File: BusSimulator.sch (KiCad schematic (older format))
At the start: 14 parts, among them U1 MPM3620, U2 MPM3620

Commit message: Finished 3v3 and 5V
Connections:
- net labels removed: Earth
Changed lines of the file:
@@
 	1700 1050 1700 1075
 $Comp
-L +5V #PWR06
+L +5V #PWR05
 U 1 1 59FAA2C5
 P 2350 2650
-F 0 "#PWR06" H 2350 2500 50  0001 C CNN
+F 0 "#PWR05" H 2350 2500 50  0001 C CNN
 F 1 "+5V" H 2350 2790 50  0000 C CNN
 F 2 "" H 2350 2650 50  0001 C CNN
@@
 $EndComp
 $Comp
-L GNDREF #PWR07
+L GNDREF #PWR06
 U 1 1 59FAACBA
 P 1475 4425
-F 0 "#PWR07" H 1475 4175 50  0001 C CNN
+F 0 "#PWR06" H 1475 4175 50  0001 C CNN
 F 1 "GNDREF" H 1475 4275 50  0000 C CNN
 F 2 "" H 1475 4425 50  0001 C CNN
@@
 $EndComp
 $Comp
-L GNDA #PWR08
+L GNDA #PWR07
 U 1 1 59FAACCC
 P 2300 6850
-F 0 "#PWR08" H 2300 6600 50  0001 C CNN
+F 0 "#PWR07" H 2300 6600 50  0001 C CNN
 F 1 "GNDA" H 2300 6700 50  0000 C CNN
 F 2 "" H 2300 6850 50  0001 C CNN
@@
 $EndComp
 $Comp
-L GNDA #PWR09
+L GNDA #PWR08
 U 1 1 59FAACD8
 P 950 6100
-F 0 "#PWR09" H 950 5850 50  0001 C CNN
+F 0 "#PWR08" H 950 5850 50  0001 C CNN
 F 1 "GNDA" H 950 5950 50  0000 C CNN
 F 2 "" H 950 6100 50  0001 C CNN
@@
 	1875 4800 2075 4800
 $Comp
-L GNDA #PWR010
+L GNDA #PWR09
 U 1 1 59FAACFB
 P 2450 4850
-F 0 "#PWR010" H 2450 4600 50  0001 C CNN
+F 0 "#PWR09" H 2450 4600 50  0001 C CNN
 F 1 "GNDA" H 2450 4700 50  0000 C CNN
 F 2 "" H 2450 4850 50  0001 C CNN
@@
 $EndComp
 $Comp
-L Earth #PWR011
-U 1 1 59FAAD09
-P 2150 6400
-F 0 "#PWR011" H 2150 6150 50  0001 C CNN
-F 1 "Earth" H 2150 6250 50  0001 C CNN
-F 2 "" H 2150 6400 50  0001 C CNN
-F 3 "" H 2150 6400 50  0001 C CNN
-	1    2150 6400
-	1    0    0    -1
-$EndComp
-$Comp
 L CAPH C3
 U 1 1 59FAAD0F
@@
 	0    1    1    0
 $EndComp
-$Comp
-L Earth #PWR012
-U 1 1 59FAAD15
-P 1475 4050
-F 0 "#PWR012" H 1475 3800 50  0001 C CNN
-F 1 "Earth" H 1475 3900 50  0001 C CNN
-F 2 "" H 1475 4050 50  0001 C CNN
-F 3 "" H 1475 4050 50  0001 C CNN
-	1    1475 4050
-	1    0    0    -1
-$EndComp
 Wire Wire Line
 	1650 4075 1650 4050
-Wire Wire Line
-	1650 4050 1475 4050
-$Comp
-L +3.3V #PWR013
+$Comp
+L +3.3V #PWR010
 U 1 1 59FAAF36
 P 2300 5650
-F 0 "#PWR013" H 2300 5500 50  0001 C CNN
+F 0 "#PWR010" H 2300 5500 50  0001 C CNN
 F 1 "+3.3V" H 2300 5790 50  0000 C CNN
 F 2 "" H 2300 5650 50  0001 C CNN
@@
 PCE3900CT-ND
 $Comp
-L GNDREF #PWR014
+L GNDREF #PWR011
 U 1 1 59FACA7B
 P 2650 2400
-F 0 "#PWR014" H 2650 2150 50  0001 C CNN
+F 0 "#PWR011" H 2650 2150 50  0001 C CNN
 F 1 "GNDREF" H 2650 2250 50  0000 C CNN
 F 2 "" H 2650 2400 50  0001 C CNN
@@
 	2200 2400 2650 2400
 $Comp
-L GNDREF #PWR015
+L GNDREF #PWR012
 U 1 1 59FACBAF
 P 2700 5350
-F 0 "#PWR015" H 2700 5100 50  0001 C CNN
+F 0 "#PWR012" H 2700 5100 50  0001 C CNN
 F 1 "GNDREF" H 2700 5200 50  0000 C CNN
 F 2 "" H 2700 5350 50  0001 C CNN
@@
 	2500 5350 2700 5350
 $Comp
-L GNDREF #PWR016
+L GNDREF #PWR013
 U 1 1 59FACE9C
 P 2200 3400
-F 0 "#PWR016" H 2200 3150 50  0001 C CNN
+F 0 "#PWR013" H 2200 3150 50  0001 C CNN
 F 1 "GNDREF" H 2200 3250 50  0000 C CNN
 F 2 "" H 2200 3400 50  0001 C CNN
@@
 $EndComp
 $Comp
-L GNDREF #PWR?
+L GNDREF #PWR014
 U 1 1 59FAD007
 P 1500 1050
-F 0 "#PWR?" H 1500 800 50  0001 C CNN
+F 0 "#PWR014" H 1500 800 50  0001 C CNN
 F 1 "GNDREF" H 1500 900 50  0000 C CNN
 F 2 "" H 1500 1050 50  0001 C CNN
@@
 Wire Wire Line
 	1500 1050 1700 1050
+$Comp
+L GNDREF #PWR015
+U 1 1 59FB82F0
+P 1450 4050
+F 0 "#PWR015" H 1450 3800 50  0001 C CNN
+F 1 "GNDREF" H 1450 3900 50  0000 C CNN
+F 2 "" H 1450 4050 50  0001 C CNN
+F 3 "" H 1450 4050 50  0001 C CNN
+	1    1450 4050
+	1    0    0    -1
+$EndComp
+Wire Wire Line
+	1650 4050 1450 4050
+$Comp
+L GNDREF #PWR016
+U 1 1 59FB843A
+P 2150 6400
+F 0 "#PWR016" H 2150 6150 50  0001 C CNN
+F 1 "GNDREF" H 2150 6250 50  0000 C CNN
+F 2 "" H 2150 6400 50  0001 C CNN
+F 3 "" H 2150 6400 50  0001 C CNN
+	1    2150 6400
+	1    0    0    -1
+$EndComp
 $EndSCHEMATC

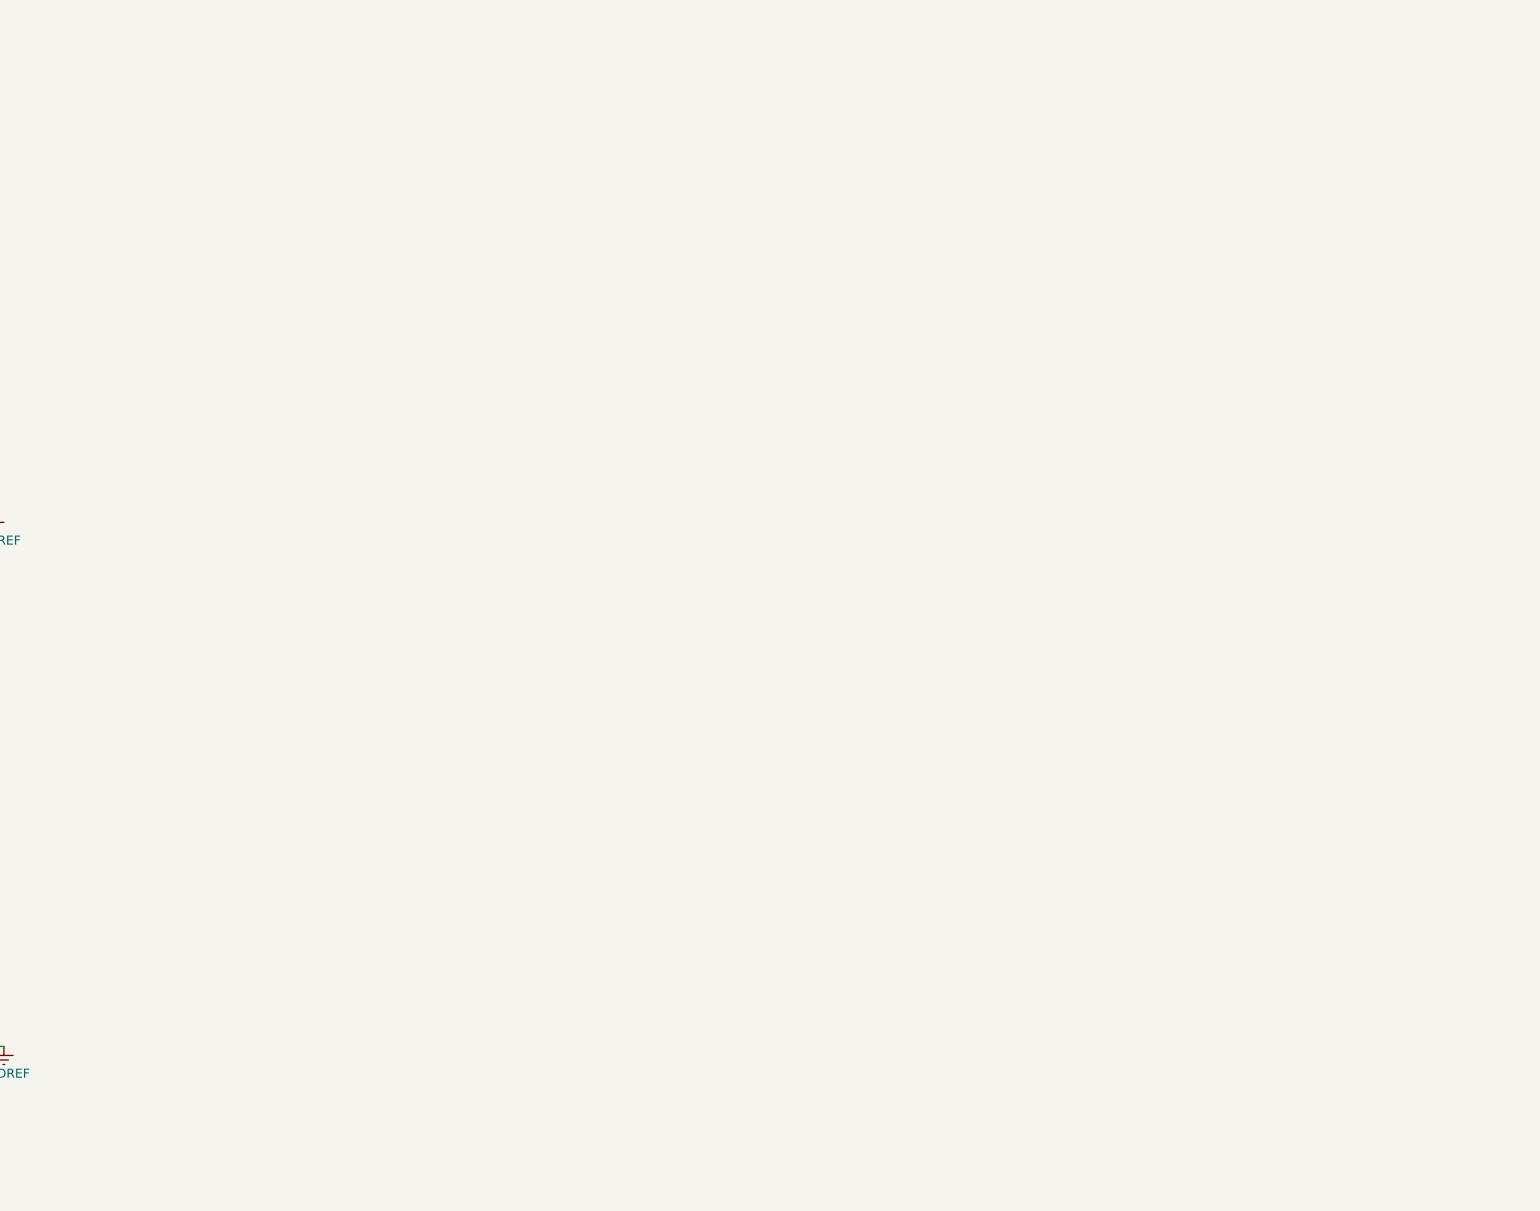
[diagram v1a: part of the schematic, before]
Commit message: Add mCOM connector to library and schematic
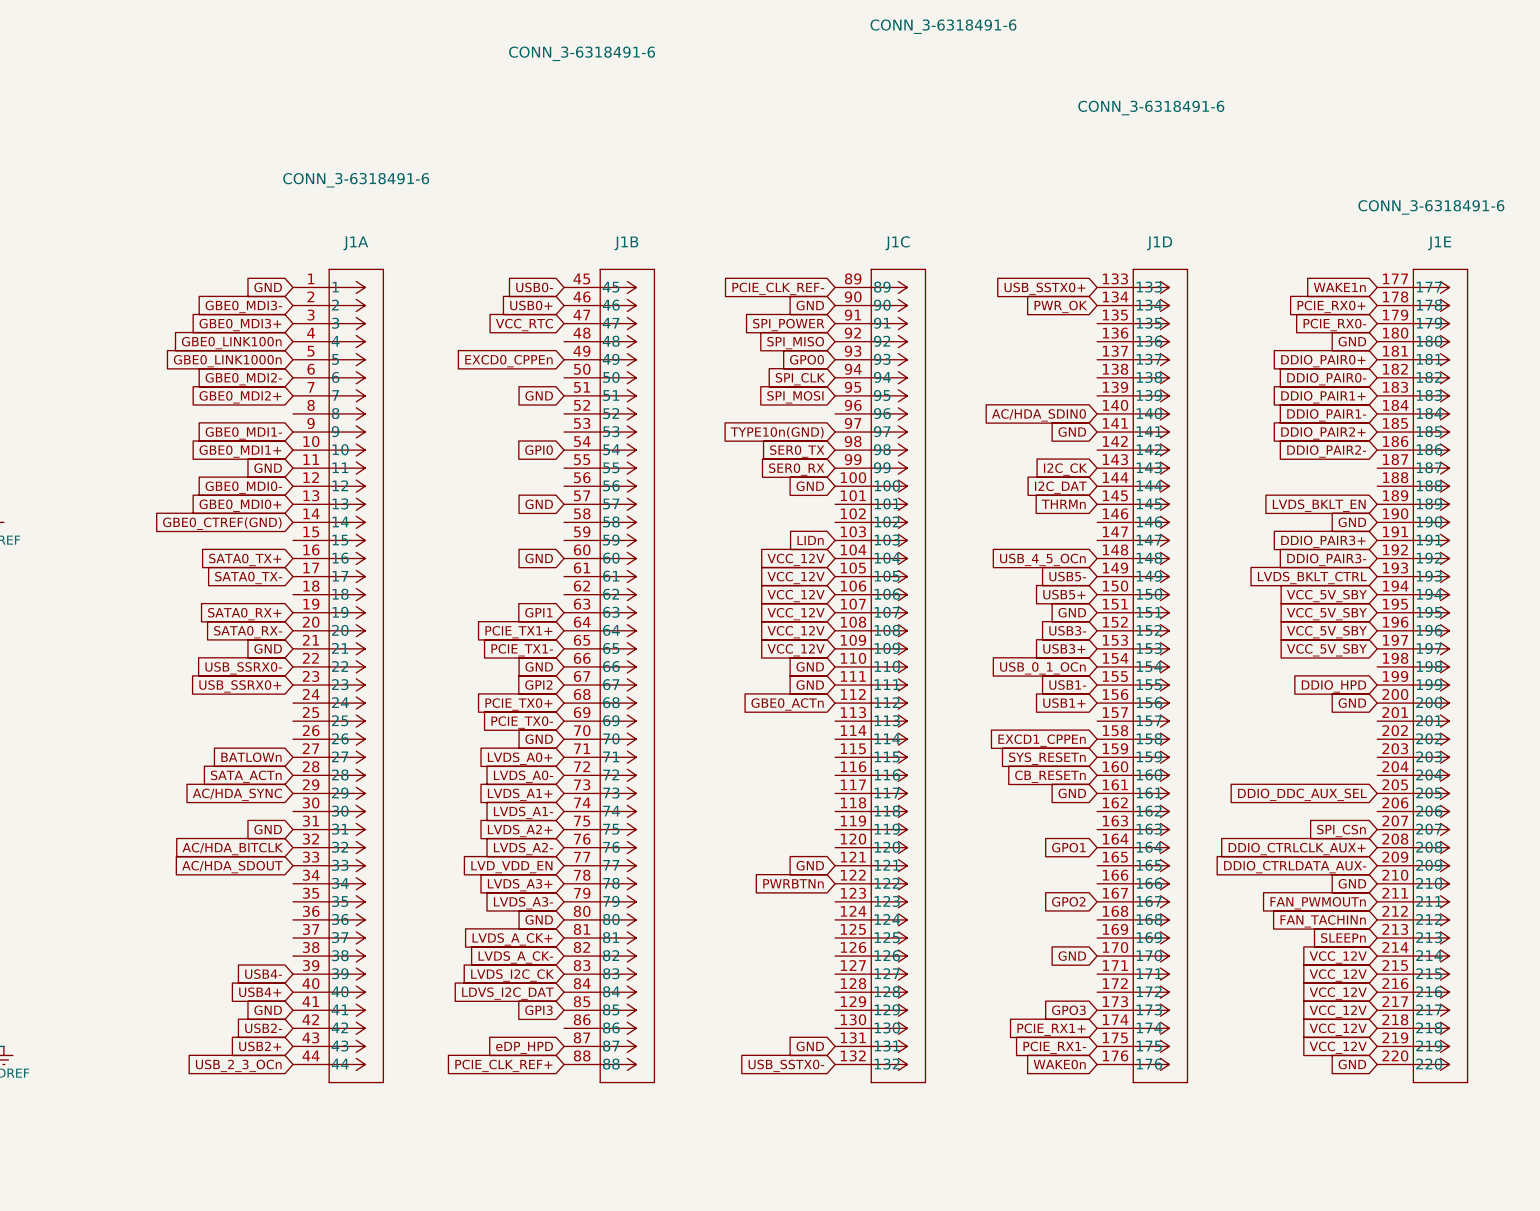
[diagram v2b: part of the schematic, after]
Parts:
- added J1: CONN_3-6318491-6, CONN_3-6318491-6, symbol CONN_3-6318491-6
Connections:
- net labels added: AC/HDA_BITCLK, AC/HDA_SDIN0, AC/HDA_SDOUT, AC/HDA_SYNC, BATLOWn, CB_RESETn, DDIO_CTRLCLK_AUX+, DDIO_CTRLDATA_AUX-, DDIO_DDC_AUX_SEL, DDIO_HPD, DDIO_PAIR0+, DDIO_PAIR0-, DDIO_PAIR1+, DDIO_PAIR1-, DDIO_PAIR2+, DDIO_PAIR2-, DDIO_PAIR3+, DDIO_PAIR3-, EXCD0_CPPEn, EXCD1_CPPEn, FAN_PWMOUTn, FAN_TACHINn, GBE0_ACTn, GBE0_CTREF(GND), GBE0_LINK1000n, GBE0_LINK100n, GBE0_MDI0+, GBE0_MDI0-, GBE0_MDI1+, GBE0_MDI1-, GBE0_MDI2+, GBE0_MDI2-, GBE0_MDI3+, GBE0_MDI3-, GND, GPI0, GPI1, GPI2, GPI3, GPO0, GPO1, GPO2, GPO3, I2C_CK, I2C_DAT, LDVS_I2C_DAT, LIDn, LVDS_A0+, LVDS_A0-, LVDS_A1+, LVDS_A1-, LVDS_A2+, LVDS_A2-, LVDS_A3+, LVDS_A3-, LVDS_A_CK+, LVDS_A_CK-, LVDS_BKLT_CTRL, LVDS_BKLT_EN, LVDS_I2C_CK, LVD_VDD_EN, PCIE_CLK_REF+, PCIE_CLK_REF-, PCIE_RX0+, PCIE_RX0-, PCIE_RX1+, PCIE_RX1-, PCIE_TX0+, PCIE_TX0-, PCIE_TX1+, PCIE_TX1-, PWRBTNn, PWR_OK, SATA0_RX+, SATA0_RX-, SATA0_TX+, SATA0_TX-, SATA_ACTn, SER0_RX, SER0_TX, SLEEPn, SPI_CLK, SPI_CSn, SPI_MISO, SPI_MOSI, SPI_POWER, SYS_RESETn, THRMn, TYPE10n(GND), USB0+, USB0-, USB1+, USB1-, USB2+, USB2-, USB3+, USB3-, USB4+, USB4-, USB5+, USB5-, USB_0_1_OCn, USB_2_3_OCn, USB_4_5_OCn, USB_SSRX0+, USB_SSRX0-, USB_SSTX0+, USB_SSTX0-, VCC_12V, VCC_5V_SBY, VCC_RTC, WAKE0n, WAKE1n, eDP_HPD

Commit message: POWER SUPPLY STUFF
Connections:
- net labels added: +12V
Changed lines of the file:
@@
 Text GLabel 10300 5450 0    51   Input ~ 0
 GND
+$Comp
+L +12V #PWR?
+U 1 1 5A040DA3
+P 1700 1350
+F 0 "#PWR?" H 1700 1200 50  0001 C CNN
+F 1 "+12V" H 1700 1490 50  0000 C CNN
+F 2 "" H 1700 1350 50  0001 C CNN
+F 3 "" H 1700 1350 50  0001 C CNN
+	1    1700 1350
+	0    -1   -1   0
+$EndComp
+$Comp
+L +12V #PWR?
+U 1 1 5A040EAE
+P 1650 4350
+F 0 "#PWR?" H 1650 4200 50  0001 C CNN
+F 1 "+12V" H 1650 4490 50  0000 C CNN
+F 2 "" H 1650 4350 50  0001 C CNN
+F 3 "" H 1650 4350 50  0001 C CNN
+	1    1650 4350
+	0    -1   -1   0
+$EndComp
 $EndSCHEMATC

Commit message: schematic build voltage sense
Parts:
- added C?: 1uF Electrolytic, BusSimulator:C22, symbol CAPH
- added C?: .1uF ceramic, BusSimulator:C22, symbol CAPH
- added J2: OSTTA024163, SHDR2W100P0X508_1X2_1086X900X1300P, symbol OSTTA024163
- added R? (x3): 10k, symbol R
- added R?: 30k, symbol R
- added U?: ADC128D818CIMTX, symbol ADC128D818CIMTX
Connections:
- net labels added: Reg0d
- wire segments 50 -> 61
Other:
- moved on the sheet: C1, C2, C3, C4, J1A, J1B, J1C, J1D, J1E, R1, R2, R3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

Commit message: opamp stuff
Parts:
- added U?: MCP6H04-E/SL, SOIC14_SL, symbol MCP6H04-E/SL
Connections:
- net labels added: +2.5V, +3V, VOutC, VoutA, VoutB, VoutC, VoutD
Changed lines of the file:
@@
 LIBS:symbols
 LIBS:OSTTA024163
+LIBS:MCP6H04-E
 LIBS:BusSimulator-cache
 EELAYER 25 0
@@
 	1    0    0    -1
 $EndComp
+$Comp
+L MCP6H04-E/SL U?
+U 1 1 5A0443F0
+P 5100 4250
+F 0 "U?" H 6000 4650 60  0000 C CNN
+F 1 "MCP6H04-E/SL" H 6000 4550 60  0000 C CNN
+F 2 "SOIC14_SL" H 6000 4490 60  0001 C CNN
+F 3 "" H 5100 4250 60  0000 C CNN
+	1    5100 4250
+	1    0    0    -1
+$EndComp
+Text GLabel 6900 4250 2    60   Input ~ 0
+VoutA
+Text GLabel 6900 4350 2    60   Input ~ 0
+VoutB
+Text GLabel 6900 4450 2    60   Input ~ 0
+VoutC
+Text GLabel 6900 4550 2    60   Input ~ 0
+VoutD
+$Comp
+L +5V #PWR?
+U 1 1 5A04477C
+P 5100 5350
+F 0 "#PWR?" H 5100 5200 50  0001 C CNN
+F 1 "+5V" H 5100 5490 50  0000 C CNN
+F 2 "" H 5100 5350 50  0001 C CNN
+F 3 "" H 5100 5350 50  0001 C CNN
+	1    5100 5350
+	1    0    0    -1
+$EndComp
+$Comp
+L GNDREF #PWR?
+U 1 1 5A0447C8
+P 6900 4950
+F 0 "#PWR?" H 6900 4700 50  0001 C CNN
+F 1 "GNDREF" H 6900 4800 50  0000 C CNN
+F 2 "" H 6900 4950 50  0001 C CNN
+F 3 "" H 6900 4950 50  0001 C CNN
+	1    6900 4950
+	1    0    0    -1
+$EndComp
+Text GLabel 4500 6150 2    60   Input ~ 0
++3.3V
+Text GLabel 5100 4350 0    60   Input ~ 0
++3.3V
+Text GLabel 5100 4250 0    60   Input ~ 0
+VoutA
+Text GLabel 5100 4450 0    60   Input ~ 0
+VoutB
+Text GLabel 4500 3150 2    60   Input ~ 0
++2.5V
+Text GLabel 5100 4550 0    60   Input ~ 0
++2.5V
+Text GLabel 5150 1750 2    60   Input ~ 0
++3V
+Text GLabel 5100 4750 0    60   Input ~ 0
++3V
+Text GLabel 5100 4650 0    60   Input ~ 0
+VoutC
+Text GLabel 5250 3100 0    60   Input ~ 0
+VoutA
+Text GLabel 5250 3000 0    60   Input ~ 0
+VoutB
+Text GLabel 5250 2900 0    60   Input ~ 0
+VOutC
+Text GLabel 5250 2800 0    60   Input ~ 0
+VoutD
 $EndSCHEMATC

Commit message: ADDED LOGO
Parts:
- added SHIELD1: ARDUINO_DUE_SHIELD, FT:ARDUINO_DUE_SHIELD, symbol ARDUINO_DUE_SHIELD
- added U5: ISO1540DR, D8, symbol ISO1540DR
- gave numbers to parts that had none: 8
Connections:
- net labels added: +3.3VA, SCLADC, SDASDC
- wire segments 61 -> 74
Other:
- moved on the sheet: J1A, J1B, J1C, J1D, J1E

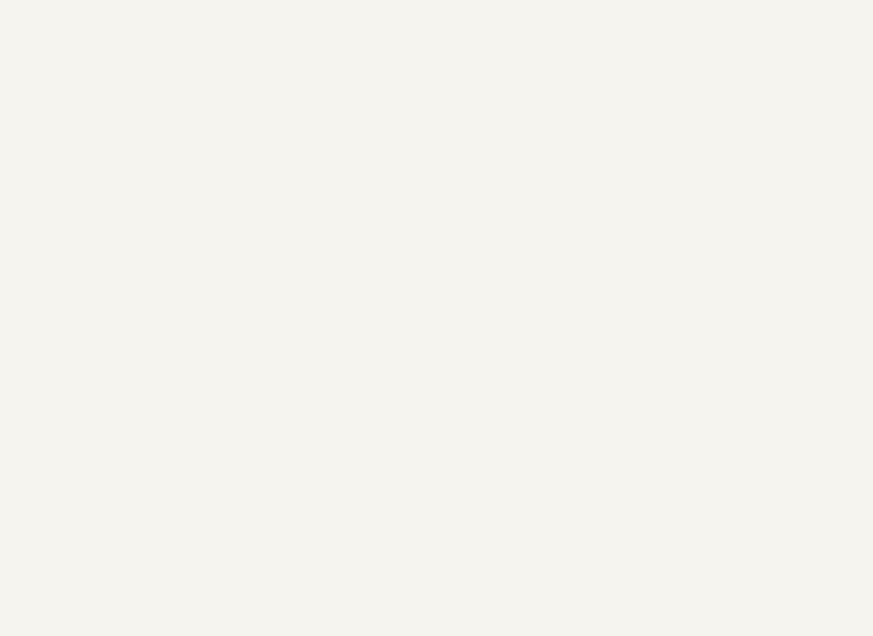
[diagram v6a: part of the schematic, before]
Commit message: Add isloator
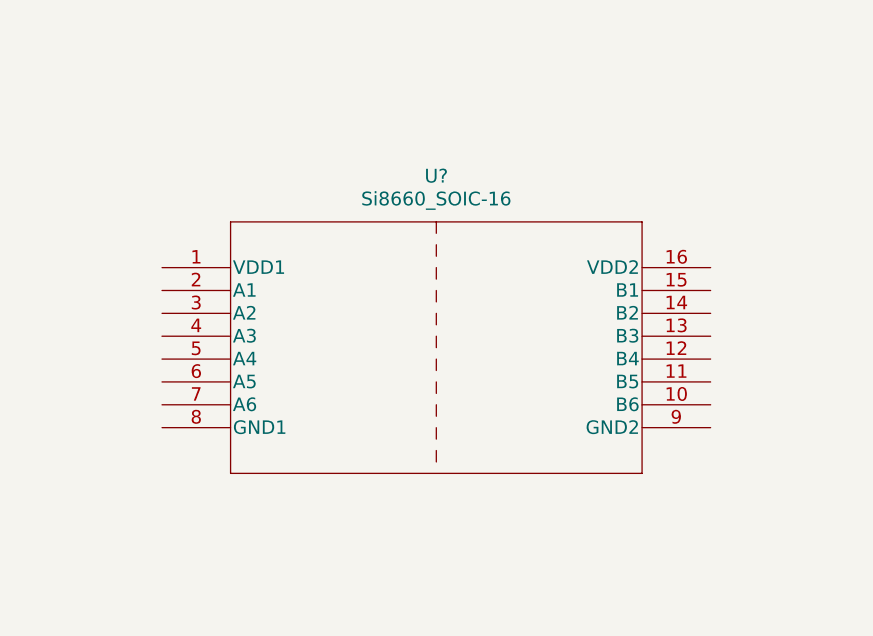
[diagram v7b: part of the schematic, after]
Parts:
- added U?: Si8660_SOIC-16, SOIC-16, symbol Si8660_SOIC-16
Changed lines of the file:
@@
 Wire Wire Line
 	13100 4550 13100 4450
+$Comp
+L Si8660_SOIC-16 U?
+U 1 1 5A04195A
+P 15550 4350
+F 0 "U?" H 16750 4750 60  0000 C CNN
+F 1 "Si8660_SOIC-16" H 16750 4650 60  0000 C CNN
+F 2 "SOIC-16" H 16750 4590 60  0001 C CNN
+F 3 "" H 15550 4350 60  0000 C CNN
+	1    15550 4350
+	1    0    0    -1
+$EndComp
 $EndSCHEMATC
